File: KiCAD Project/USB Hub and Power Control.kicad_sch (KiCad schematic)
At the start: 44 parts, among them J4 USB1030-GF-P-B-B, J5 USB1035-GF-P-0-B-B, J6 USB1035-GF-P-0-B-B, U4 TUSB4041IPAPR

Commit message: v1.0.0 RC2
Build candidate 2
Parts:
- J5, J6: Spec (none) -> USB Connectors USB A Skt, TH, GF, USB-A 2.0
- U4: Spec (none) -> TUSB4041IPAPR
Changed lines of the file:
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@@
 			)
 		)
-		(property "Spec" ""
+		(property "Spec" "USB Connectors USB A Skt, TH, GF, USB-A 2.0"
 			(at 233.68 68.58 0)
 			(effects
@@
 			)
 		)
+		(property "Spec" "TUSB4041IPAPR"
+			(at 63.5 101.6 0)
+			(effects
+				(font
+					(size 1.27 1.27)
+				)
+			)
+		)
 		(pin "1"
 		)
@@
 			)
 		)
-		(property "Spec" ""
+		(property "Spec" "USB Connectors USB A Skt, TH, GF, USB-A 2.0"
 			(at 233.68 132.08 0)
 			(effects

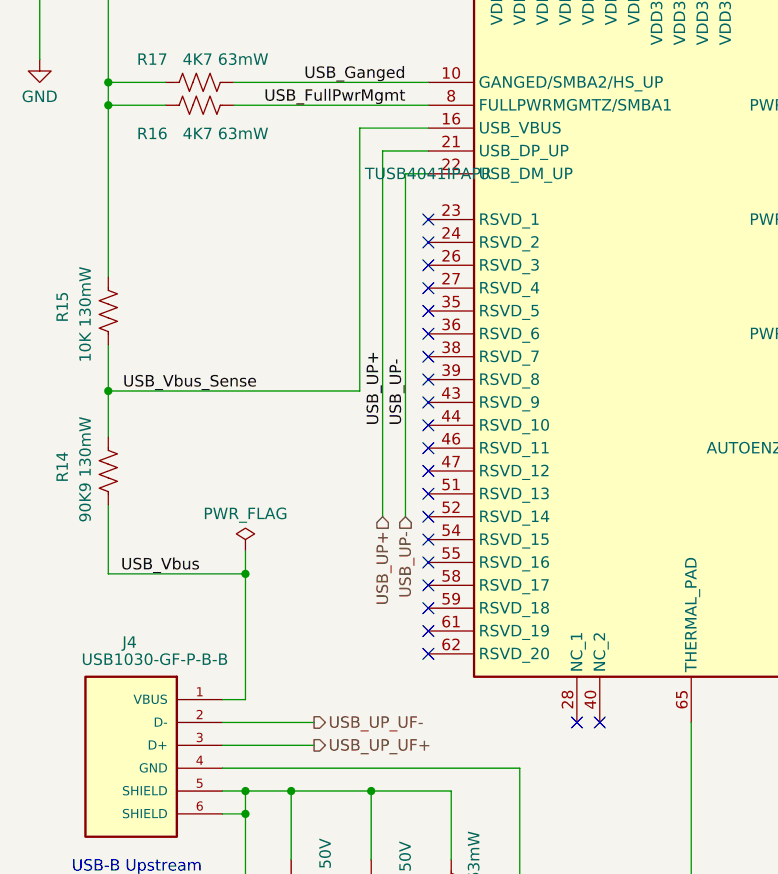
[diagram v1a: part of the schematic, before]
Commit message: v1.0.0 RC3
Minor change to upstream USB port to connect Vbus to ESD protection vice on-board 5V.
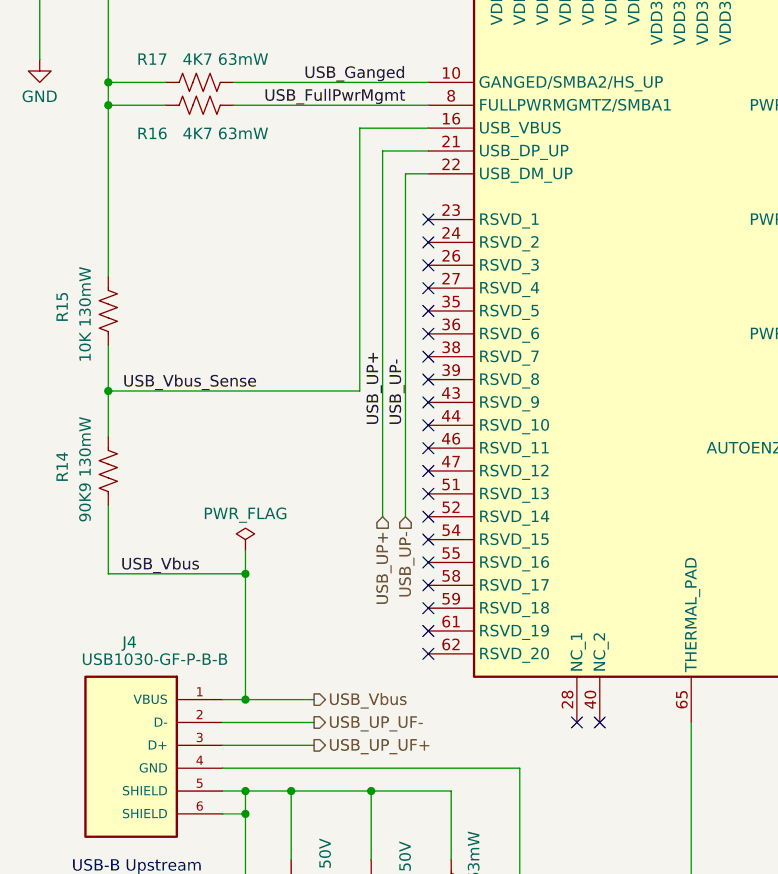
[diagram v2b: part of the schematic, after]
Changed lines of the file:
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@@
 		(title "1026 RPi Power Hat")
 		(date "2025-04-11")
-		(rev "1")
+		(rev "1.0.0 RC3")
 		(company "Dan Wilson")
 		(comment 1 "Copyright © 2025 Dan Wilson")
@@
 	)
 	(junction
+		(at 43.18 160.02)
+		(diameter 0)
+		(color 0 0 0 0)
+	)
+	(junction
 		(at 81.28 41.91)
 		(diameter 0)
@@
 	(wire
 		(pts
+			(xy 43.18 160.02) (xy 50.8 160.02)
+		)
+		(stroke
+			(width 0)
+			(type default)
+		)
+	)
+	(wire
+		(pts
 			(xy 55.88 96.52) (xy 63.5 96.52)
 		)
@@
 		)
 	)
+	(hierarchical_label "USB_Vbus"
+		(shape output)
+		(at 50.8 160.02 0)
+		(effects
+			(font
+				(size 1.27 1.27)
+			)
+			(justify left)
+		)
+	)
 	(hierarchical_label "USB_DS3_UF+"
 		(shape input)
@@
 					(size 1.27 1.27)
 				)
+				(hide yes)
 			)
 		)

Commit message: v1.0.0A
Moved all symbols, footprints, and 3D models to local project-specific libraries in /KiCAD Project/Libraries.
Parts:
- C17, C18, C19, C20, C22, C23, C24, C25, C26, C27, C28, C30, C31, C32, C33, C34, C35: footprint Capacitor_SMD:C_0402_1005Metric -> 1026-3D:C_0402_1005Metric; symbol Device:C -> 1026-3D:C
- C21, C29: footprint Capacitor_SMD:C_0805_2012Metric -> 1026-3D:C_0805_2012Metric; symbol Device:C -> 1026-3D:C
- C36: footprint Capacitor_SMD:C_0603_1608Metric -> 1026-3D:C_0603_1608Metric; symbol Device:C -> 1026-3D:C
- FB1, FB2: footprint DW_Passives:[FB] Murata BLM15PX221SZ1D -> 1026-3D:[FB] Murata BLM15PX221SZ1D; symbol DW_Passives:[FB] Murata BLM15PX221SZ1D 220ohm 800mA -> 1026-3D:[FB] Murata BLM15PX221SZ1D 220ohm 800mA
- J4: footprint DW_Connectors:[J] GCT USB-B 2.0 Connector PCB USB1030-GF-P-B-B -> 1026-3D:[J] GCT USB-B 2.0 Connector PCB USB1030-GF-P-B-B; symbol DW_Connectors:[J] GCT USB-B 2.0 Connector PCB USB1030-GF-P-B-B -> 1026-3D:[J] GCT USB-B 2.0 Connector PCB USB1030-GF-P-B-B
- J5, J6: footprint DW_Connectors:[J] GCT USB-A x2 2.0 Connector USB1035-GF-P-0-B-B -> 1026-3D:[J] GCT USB-A x2 2.0 Connector USB1035-GF-P-0-B-B; symbol DW_Connectors:[J] GCT USB-A x2 2.0 PCB USB1035-GF-P-0-B-B -> 1026-3D:[J] GCT USB-A x2 2.0 PCB USB1035-GF-P-0-B-B
- R14, R15, R16, R17, R18, R19, R20, R21, R22, R23, R24, R25, R26, R27, R29, R30, R31, R32: footprint Resistor_SMD:R_0402_1005Metric -> 1026-3D:R_0402_1005Metric; symbol Device:R_US -> 1026-3D:R_US
- U4: footprint DW_Semiconductors:[U] Texas Inst USB 2.0 Hub Controller TUSB4041I QFP50P1200X1200X120-65N -> 1026-3D:[U] Texas Inst USB 2.0 Hub Controller TUSB4041I QFP50P1200X1200X120-65N; symbol DW_Semiconductors:[U] Texas Inst TUSB4041IPAPR USB 2.0 Hub Controller -> 1026-3D:[U] Texas Inst TUSB4041IPAPR USB 2.0 Hub Controller
